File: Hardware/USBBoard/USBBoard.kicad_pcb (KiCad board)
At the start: 2 copper layers, 27.9 x 38.1 mm, 22 parts, among them J1 USB_C_Receptacle_USB2.0, J2 POWERBOARD, Q3 BC846, Q4 BC846, U1 CH340C

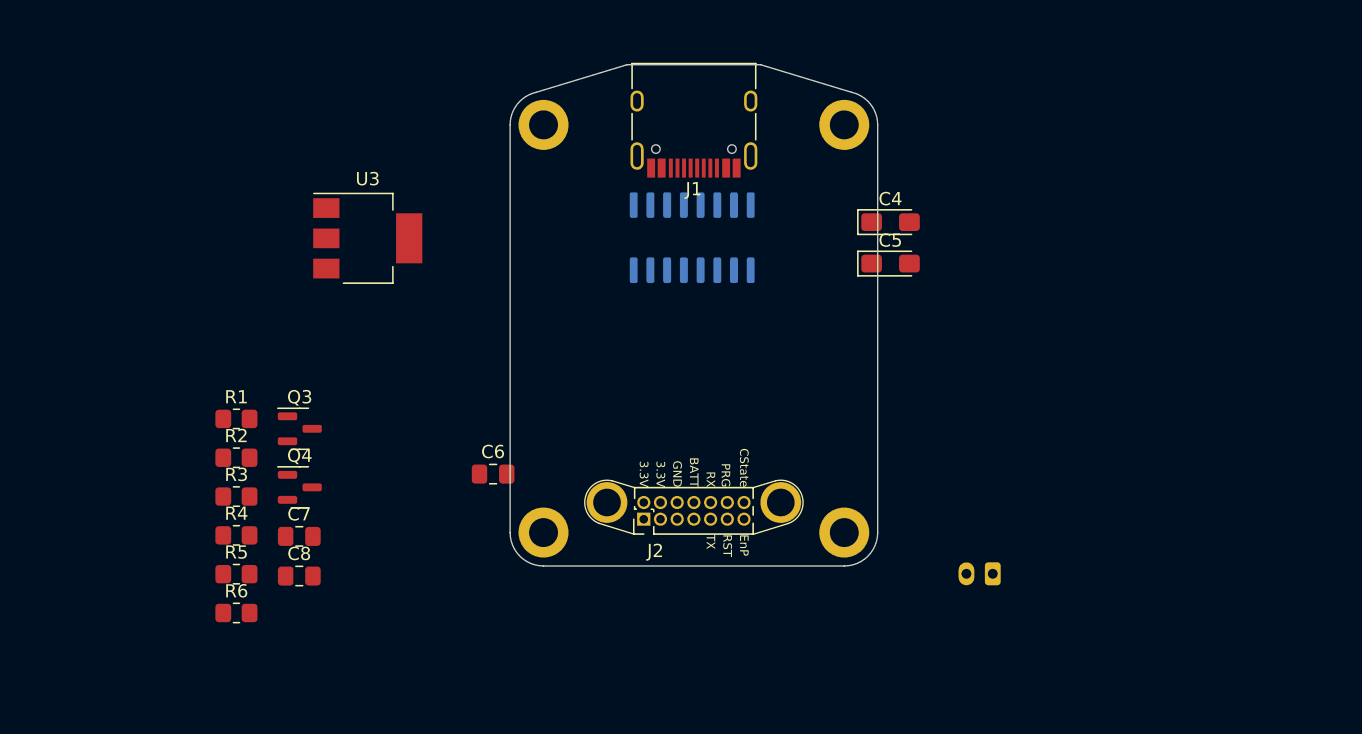
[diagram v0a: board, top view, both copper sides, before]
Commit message: Fix grouping issue on USBBoard
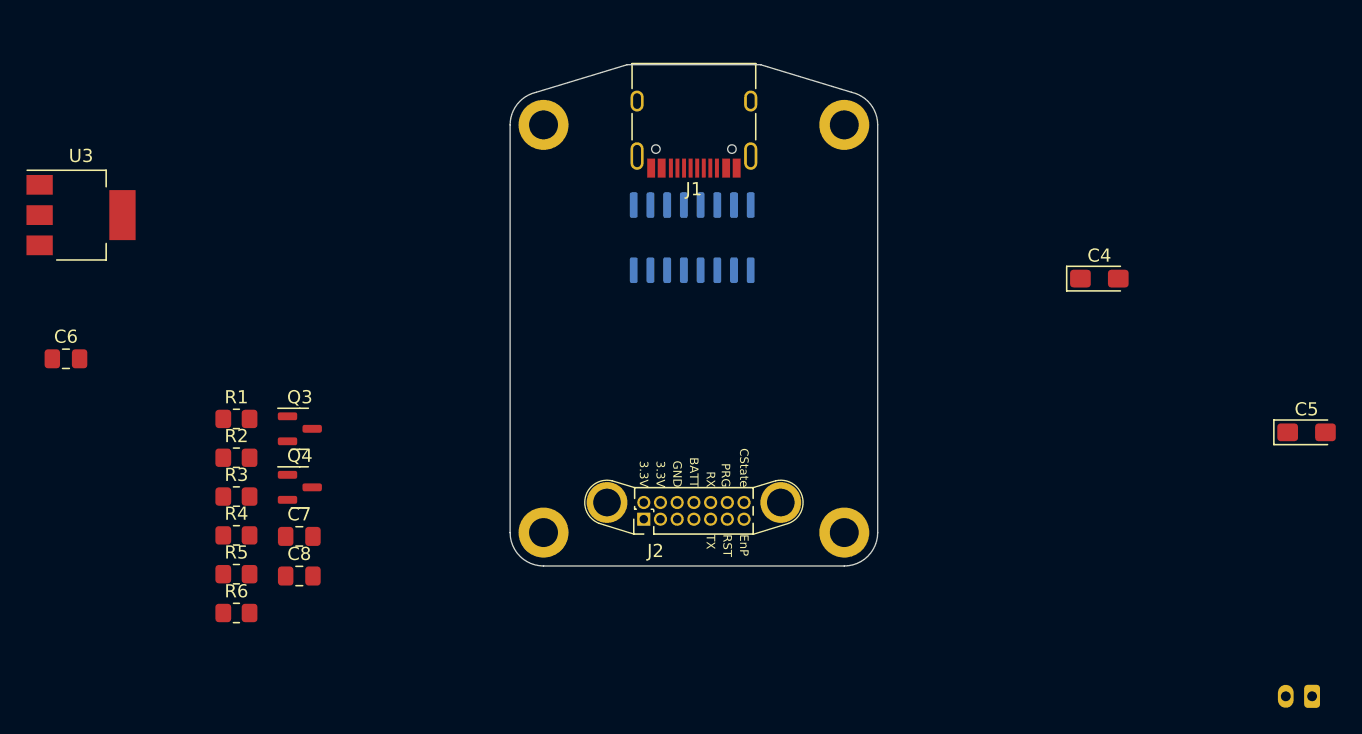
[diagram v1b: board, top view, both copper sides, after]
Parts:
- moved C5 34.1 mm to (46.6, -5.33)
- moved C6 33.6 mm to (-47.7, -10.9)
- moved BT1 26.0 mm to (47.0, 14.7)
- moved U3 21.9 mm to (-46.6, -21.8)
- moved C4 16.4 mm to (30.8, -17.0)
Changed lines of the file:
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@@
   )
   (footprint "Capacitor_SMD:C_0805_2012Metric_Pad1.18x1.45mm_HandSolder" (layer "F.Cu")
-    (at -15.2615 -2.159)
+    (at -47.7305 -10.922)
     (descr "Capacitor SMD 0805 (2012 Metric), square (rectangular) end terminal, IPC_7351 nominal with elongated pad for handsoldering. (Body size source: IPC-SM-782 page 76, https://www.pcb-3d.com/wordpress/wp-content/uploads/ipc-sm-782a_amendment_1_and_2.pdf, https://docs.google.com/spreadsheets/d/1BsfQQcO9C6DZCsRaXUlFlo91Tg2WpOkGARC1WS5S8t0/edit?usp=sharing), generated with kicad-footprint-generator")
     (tags "capacitor handsolder")
@@
   )
   (footprint "Capacitor_Tantalum_SMD:CP_EIA-3216-18_Kemet-A_Pad1.58x1.35mm_HandSolder" (layer "F.Cu")
-    (at 14.9455 -21.311)
+    (at 30.8205 -17.018)
     (descr "Tantalum Capacitor SMD Kemet-A (3216-18 Metric), IPC_7351 nominal, (Body size from: http://www.kemet.com/Lists/ProductCatalog/Attachments/253/KEM_TC101_STD.pdf), generated with kicad-footprint-generator")
     (tags "capacitor tantalum")
@@
   )
   (footprint "Package_TO_SOT_SMD:SOT-223" (layer "F.Cu")
-    (at -24.79 -20.08)
+    (at -46.584 -21.844)
     (descr "module CMS SOT223 4 pins")
     (tags "CMS SOT")
@@
   )
   (footprint "Capacitor_Tantalum_SMD:CP_EIA-3216-18_Kemet-A_Pad1.58x1.35mm_HandSolder" (layer "F.Cu")
-    (at 14.9455 -18.161)
+    (at 46.5685 -5.334)
     (descr "Tantalum Capacitor SMD Kemet-A (3216-18 Metric), IPC_7351 nominal, (Body size from: http://www.kemet.com/Lists/ProductCatalog/Attachments/253/KEM_TC101_STD.pdf), generated with kicad-footprint-generator")
     (tags "capacitor tantalum")
@@
   )
   (footprint "Connector_JST:JST_PH_B2B-PH-K_1x02_P2.00mm_Vertical" (layer "B.Cu")
-    (at 22.717 5.419 180)
+    (at 46.99 14.732 180)
     (descr "JST PH series connector, B2B-PH-K (http://www.jst-mfg.com/product/pdf/eng/ePH.pdf), generated with kicad-footprint-generator")
     (tags "connector JST PH side entry")
@@
   (gr_arc (start -11.43 4.826) (mid -13.226051 4.082051) (end -13.97 2.286)
     (stroke (width 0.1) (type default)) (layer "Edge.Cuts"))
-  (group "" (id 6e419160-7dae-4afb-b36b-74f0ed6fae22)
+  (group "" (id 5ae80237-eeec-4c41-a94c-e3d590e48130)
     (members
-      9fc7ae75-cb9d-483a-b104-ba5820dbb04a
-      e5d91561-4228-46c9-98d3-a81c8428babf
-    )
-  )
-  (group "" (id 136651ce-4058-401b-809c-dfe45570d33c)
+      6c59bba5-8c0c-46e1-a3d5-0e7b95a1a711
+      f1650c99-eb59-4066-9fe7-7616f7fdb038
+      f17f2430-3204-47c0-92a9-38e1003b621e
+      fbade2e1-fbd6-46db-8691-6e243b1c1a97
+    )
+  )
+  (group "" (id b35aa1eb-7377-47d7-91fa-bf5fa3904c37)
     (members
       1b8b4129-4e0f-4907-821b-debf22a0e586
+      488da1a5-a669-4554-aef4-275d1cf42de7
       595b5577-f80f-4536-a76b-1c94b30a4fa7
       5e652a05-7d76-4dde-98b5-c17f953701ce
-      6c59bba5-8c0c-46e1-a3d5-0e7b95a1a711
-      6e419160-7dae-4afb-b36b-74f0ed6fae22
       862abcaa-c0cf-4b10-8eb4-3672ba84206c
-      863f15d1-b69c-4074-8bb0-5c7c9043105a
-      a2b0aa00-3413-4be7-a55c-03320e35ac2b
+      a8eedac0-18a2-44b1-9eed-9e6a1d79b405
       acf0a8a8-c36b-40c5-8487-7b26d87f9816
       b8d8991f-8289-4a6e-aa6a-a7f3250879c0
       e7b52943-40c6-4bba-a188-db1fdccc1976
       f0d84bac-f7db-4423-a1fa-6e508c41df07
-      f1650c99-eb59-4066-9fe7-7616f7fdb038
-    )
-  )
+    )
+  )

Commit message: USBBoard complete
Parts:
- added C1: 100nF, Capacitor_SMD:C_0805_2012Metric_Pad1.18x1.45mm_HandSolder, F.Cu at (10.2, -18.0)
- added C10: 1uF Tantalum, Capacitor_Tantalum_SMD:CP_EIA-3216-18_Kemet-A_Pad1.58x1.35mm_HandSolder, F.Cu at (-4.85, -10.4)
- added C2: 10uF, Capacitor_SMD:C_0805_2012Metric_Pad1.18x1.45mm_HandSolder, F.Cu at (7.42, -21.0)
- added C3: 0.1uF, Capacitor_SMD:C_0805_2012Metric_Pad1.18x1.45mm_HandSolder, F.Cu at (-11.4, -21.6)
- added C9: 1uF Tantalum, Capacitor_Tantalum_SMD:CP_EIA-3216-18_Kemet-A_Pad1.58x1.35mm_HandSolder, F.Cu at (-12.1, -10.4)
- added D1: CHARGE, Diode_SMD:D_0805_2012Metric_Pad1.15x1.40mm_HandSolder, B.Cu at (6.30, -30.7)
- added D2: STBY, Diode_SMD:D_0805_2012Metric_Pad1.15x1.40mm_HandSolder, B.Cu at (-6.35, -30.7)
- added Q1: BS170F, Package_TO_SOT_SMD:SOT-23, B.Cu at (0.15, -17.5)
- added Q2: BS170F, Package_TO_SOT_SMD:SOT-23, B.Cu at (1.52, -23.3)
- added Q5: AO3401A, Package_TO_SOT_SMD:SOT-23, F.Cu at (-5.10, -14.9)
- added Q6: 2N7002, Package_TO_SOT_SMD:SOT-23, F.Cu at (-9.11, -14.9)
- added R10: 1K, Resistor_SMD:R_0805_2012Metric_Pad1.20x1.40mm_HandSolder, F.Cu at (-6.35, -30.7)
- added R11: 12K, Resistor_SMD:R_0805_2012Metric_Pad1.20x1.40mm_HandSolder, B.Cu at (0.30, -14.5)
- added R12: 12K, Resistor_SMD:R_0805_2012Metric_Pad1.20x1.40mm_HandSolder, B.Cu at (2.84, -17.4)
- added R13: 12K, Resistor_SMD:R_0805_2012Metric_Pad1.20x1.40mm_HandSolder, B.Cu at (4.22, -23.3)
- added R14: 12K, Resistor_SMD:R_0805_2012Metric_Pad1.20x1.40mm_HandSolder, B.Cu at (1.69, -20.4)
- added R15: 10K, Resistor_SMD:R_0805_2012Metric_Pad1.20x1.40mm_HandSolder, F.Cu at (-5.16, -17.7)
- added R16: 10K, Resistor_SMD:R_0805_2012Metric_Pad1.20x1.40mm_HandSolder, F.Cu at (-12.1, -15.1)
- added R17: 1K, Resistor_SMD:R_0805_2012Metric_Pad1.20x1.40mm_HandSolder, F.Cu at (-9.18, -17.7)
- added R7: 1K, Resistor_SMD:R_0805_2012Metric_Pad1.20x1.40mm_HandSolder, F.Cu at (7.24, -15.0)
- added R8: 100, Resistor_SMD:R_0805_2012Metric_Pad1.20x1.40mm_HandSolder, F.Cu at (6.24, -18.0)
- added R9: 1K, Resistor_SMD:R_0805_2012Metric_Pad1.20x1.40mm_HandSolder, F.Cu at (6.30, -30.7)
- added U2: FS8205A, Package_SO:TSSOP-8_4.4x3mm_P0.65mm, F.Cu at (10.2, -11.3)
- added U4: TC4056A, Package_SO:SOP-8_3.9x4.9mm_P1.27mm, F.Cu at (2.24, -12.4)
- added U6: DW01-P, Package_SO:TSOP-6_1.65x3.05mm_P0.95mm, F.Cu at (10.1, -15.0)
- added U7: XC6203, Package_TO_SOT_SMD:SOT-89-3, F.Cu at (-8.51, -5.44)
- BT1: moved to F.Cu
- C6: value 10uF -> 0.1uF
- Q3, Q4, R2, R3: moved to B.Cu
- U3: value ~ -> XC6203; footprint Package_TO_SOT_SMD:SOT-223 -> Package_TO_SOT_SMD:SOT-89-3
- moved BT1 51.5 mm to (10.9, -22.0), turned to 90 degrees
- moved C5 51.4 mm to (-4.88, -5.06), turned to 90 degrees
- moved R6 48.6 mm to (11.4, -6.60)
- moved R5 47.3 mm to (11.4, -4.57)
- moved R1 46.3 mm to (11.4, -2.54), turned to 180 degrees
- moved C4 44.6 mm to (-12.1, -5.06), turned to -90 degrees
- moved R4 40.4 mm to (4.08, -8.48)
- moved C6 40.1 mm to (-9.05, -21.5), turned to -90 degrees
- moved U3 39.7 mm to (-8.48, -10.8), turned to 90 degrees
- moved C7 37.3 mm to (2.26, -16.1)
- moved C8 33.4 mm to (0.28, -8.48), turned to 180 degrees
- moved R3 31.3 mm to (-8.04, -16.8)
- moved R2 26.6 mm to (-11.8, -16.8), turned to 180 degrees
- moved Q4 25.4 mm to (-7.88, -13.8), turned to -90 degrees
- moved Q3 19.8 mm to (-11.9, -13.8), turned to -90 degrees
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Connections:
- BT1 pad 2: GND -> -BATT
- C6 pad 1: +3.3V -> Net-(U1-V3)
- R5 pad 1: Net-(U4-STBY) -> STATE_STBY
- R6 pad 1: Net-(U4-CHARGE) -> STATE_CHARGE
- U1 pad 16: +3.3V -> +5V
- U1 pad 2: UC_RX -> Net-(Q1-D)
- U1 pad 3: UC_TX -> Net-(Q2-D)
- U1 pad 4: +3.3V -> Net-(U1-V3)
- U3 pad 2: +BATT -> Net-(Q5-D)
- U3 pad 3: +3.3V -> +3.3VP
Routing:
- net GND: track 0.00 -> 212.8 mm, vias 0 -> 7
- net +5V: track 0.00 -> 64.7 mm, vias 0 -> 3
- net +BATT: track 0.00 -> 59.2 mm, vias 0 -> 2
- net STATE_STBY: track 0.00 -> 56.3 mm, vias 0 -> 1
- net +3.3V: track 0.00 -> 54.3 mm, vias 0 -> 4
- net STATE_CHARGE: track 0.00 -> 40.5 mm, vias 0 -> 1
- net EnPower: track 0.00 -> 33.7 mm, vias 0 -> 1
- net UC_ID0: track 0.00 -> 33.3 mm
- net UC_TX: track 0.00 -> 32.6 mm, vias 0 -> 3
- net UC_EN: track 0.00 -> 29.1 mm
- net -BATT: track 0.00 -> 24.7 mm
- net Net-(Q2-D): track 0.00 -> 24.1 mm
- net Net-(Q1-D): track 0.00 -> 19.1 mm
- net UC_RX: track 0.00 -> 18.1 mm, vias 0 -> 1
- net USB_D-: track 0.00 -> 16.4 mm, vias 0 -> 1
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- added copper zone on B.Cu, net GND
- added copper zone on F.Cu, net GND
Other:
- board text added: "CHARGE"
- board text added: "STBY"

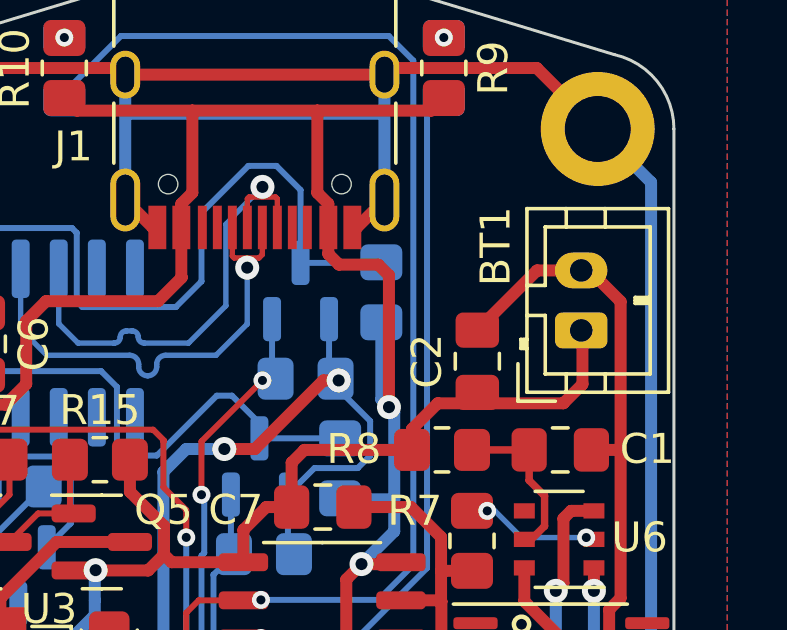
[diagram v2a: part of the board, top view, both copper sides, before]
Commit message: Library paths relative instead of absolute
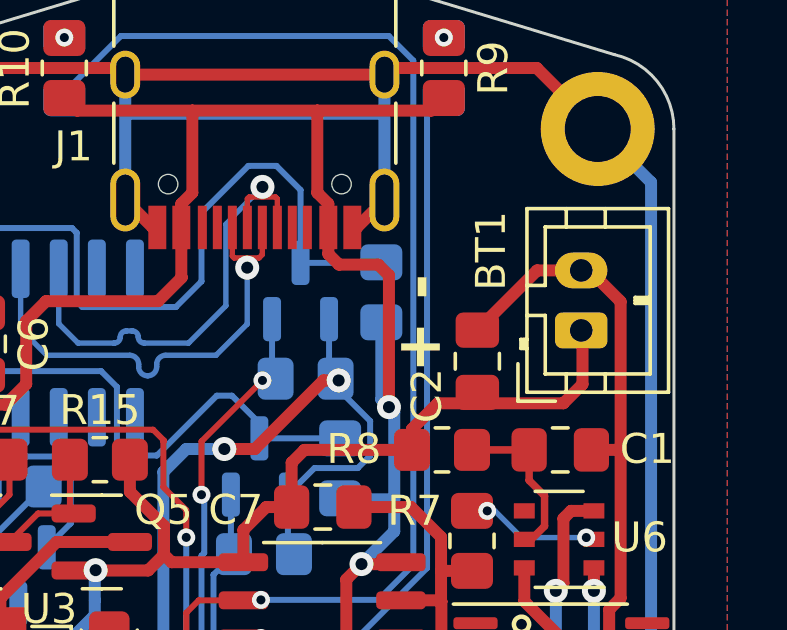
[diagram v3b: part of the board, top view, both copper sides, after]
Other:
- board text added: "+ -"
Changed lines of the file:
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@@
     (property "ki_keywords" "battery cell")
     (attr through_hole)
-    (fp_text reference "BT1" (at 2.8034 -2.8536 90) (layer "F.SilkS")
+    (fp_text reference "BT1" (at 2.651 -3.006 90) (layer "F.SilkS")
         (effects (font (size 1 1) (thickness 0.15)))
     )
@@
     (property "ki_keywords" "capacitor cap")
     (attr smd)
-    (fp_text reference "C2" (at 0 -1.68 90) (layer "F.SilkS")
+    (fp_text reference "C2" (at -1.1469 -1.68 90) (layer "F.SilkS")
         (effects (font (size 1 1) (thickness 0.15)))
     )
@@
     (effects (font (size 1 1) (thickness 0.2)) (justify bottom mirror))
   )
+  (gr_text "+ -" (at 6.35 -20.574 90) (layer "F.SilkS")
+    (effects (font (size 1.5 1.5) (thickness 0.3) bold) (justify left bottom))
+  )
   (segment (start -12.1412 -3.62305) (end -13.2162 -4.69805) (width 0.4) (layer "F.Cu") (net 1))

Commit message: USBBoard tweaks
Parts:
- moved BT1 0.64 mm to (10.9, -22.6)
- moved C1 0.64 mm to (10.2, -18.6)
- moved C2 0.64 mm to (7.42, -21.6)
- moved J1 0.64 mm to (0.00, -30.1)
- moved Q2 0.64 mm to (1.52, -23.9)
- moved R16 0.64 mm to (-12.1, -15.7)
- moved R8 0.64 mm to (6.24, -18.6)
- moved U7 0.64 mm to (-8.51, -6.07)
- moved H3 0.64 mm to (11.4, 1.65)
- moved H4 0.64 mm to (-11.4, 1.65)
- moved J2 0.64 mm to (0.00, 0.00)
- moved C10 0.63 mm to (-4.85, -11.0)
- moved C4 0.63 mm to (-12.1, -5.70)
- moved C5 0.63 mm to (-4.88, -5.70)
- moved C8 0.63 mm to (0.28, -9.11)
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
